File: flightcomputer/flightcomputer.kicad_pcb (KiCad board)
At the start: 2 copper layers, 100 x 100 mm, 48 parts, among them J1 Conn_Coaxial, J10 Conn_01x03, J11 Conn_01x03, J12 M20-6102045, J13 Conn_01x07, J2 Conn_Coaxial, J3 Conn_Coaxial, J4 Conn_Coaxial, U1 MAX-M10S, U2 LIS2MDLTR, U3 BMI088, U4 MS5607-02BA, U7 Teensy4.1, U8 LSM6DSO32TR, U9 RFM96W-433S2

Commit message: placement
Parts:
- removed D4, D5, D6: LED, LED_SMD:LED_0603_1608Metric_Pad1.05x0.95mm_HandSolder
- removed J13: Conn_01x07, Connector_Molex:Molex_SL_171971-0007_1x07_P2.54mm_Vertical
- removed R12, R13, R8: 500, Resistor_SMD:R_0603_1608Metric_Pad0.98x0.95mm_HandSolder
- removed R3, R4, R5, R6: 0, Resistor_SMD:R_0603_1608Metric_Pad0.98x0.95mm_HandSolder
- added BT1: 2998TR, HPRlibrary:BAT_2998TR, B.Cu at (69.7, 136.0)
- added C9: 1uF, Capacitor_SMD:C_0603_1608Metric_Pad1.08x0.95mm_HandSolder, F.Cu at (69.0, 111.0)
- added D10: ESD9B5.0ST5G, Diode_SMD:D_SOD-923, F.Cu at (262.4, 20.9)
- added D7: ESD9B5.0ST5G, Diode_SMD:D_SOD-923, F.Cu at (262.4, 15.0)
- added D8: ESD9B5.0ST5G, Diode_SMD:D_SOD-923, F.Cu at (262.4, 16.9)
- added D9: ESD9B5.0ST5G, Diode_SMD:D_SOD-923, F.Cu at (262.4, 18.9)
- added J5: S3B-PH-K-S-GW, HPRlibrary:S3BPHKSGW, F.Cu at (63.5, 87.0)
- added J6: S3B-PH-K-S-GW, HPRlibrary:S3BPHKSGW, F.Cu at (105.0, 132.6)
- added J7: S4B-PH-K-S_LF__SN_, HPRlibrary:S4B-PH-K-S_LF__SN_, F.Cu at (62.5, 98.0)
- added J8: S3B-PH-K-S-GW, HPRlibrary:S3BPHKSGW, F.Cu at (109.0, 79.5)
- added J9: Conn_01x06, Connector_PinHeader_2.54mm:PinHeader_1x06_P2.54mm_Vertical, F.Cu at (117.7, 122.0)
- added R14: 0, Resistor_SMD:R_0603_1608Metric_Pad0.98x0.95mm_HandSolder, F.Cu at (65.0, 127.2)
- added R15: 0, Resistor_SMD:R_0603_1608Metric_Pad0.98x0.95mm_HandSolder, F.Cu at (128.0, 83.9)
- added R16: 0, Resistor_SMD:R_0603_1608Metric_Pad0.98x0.95mm_HandSolder, F.Cu at (131.0, 83.9)
- added R17: 0, Resistor_SMD:R_0603_1608Metric_Pad0.98x0.95mm_HandSolder, F.Cu at (59.1, 110.0)
- added R7: 0, Resistor_SMD:R_0603_1608Metric_Pad0.98x0.95mm_HandSolder, F.Cu at (68.0, 127.2)
- added S1: EG1218, HPRlibrary:SW_EG1218, F.Cu at (60.0, 118.0)
- added TP10: TestPoint, Connector_PinHeader_2.54mm:PinHeader_1x01_P2.54mm_Vertical, F.Cu at (192.0, 43.2)
- added TP11: TestPoint, Connector_PinHeader_2.54mm:PinHeader_1x01_P2.54mm_Vertical, F.Cu at (192.0, 47.8)
- added TP12: TestPoint, Connector_PinHeader_2.54mm:PinHeader_1x01_P2.54mm_Vertical, F.Cu at (192.0, 52.4)
- added TP13: TestPoint, Connector_PinHeader_2.54mm:PinHeader_1x01_P2.54mm_Vertical, F.Cu at (192.0, 57.0)
- added TP14: TestPoint, Connector_PinHeader_2.54mm:PinHeader_1x01_P2.54mm_Vertical, F.Cu at (192.0, 34.0)
- added TP15: TestPoint, Connector_PinHeader_2.54mm:PinHeader_1x01_P2.54mm_Vertical, F.Cu at (115.0, 80.0)
- added TP16: TestPoint, Connector_PinHeader_2.54mm:PinHeader_1x01_P2.54mm_Vertical, F.Cu at (115.0, 75.4)
- added TP17: TestPoint, Connector_PinHeader_2.54mm:PinHeader_1x01_P2.54mm_Vertical, F.Cu at (99.0, 132.4)
- added TP18: TestPoint, Connector_PinHeader_2.54mm:PinHeader_1x01_P2.54mm_Vertical, F.Cu at (99.0, 137.0)
- added TP19: TestPoint, Connector_PinHeader_2.54mm:PinHeader_1x01_P2.54mm_Vertical, F.Cu at (70.0, 86.0)
- added TP2: TestPoint, Connector_PinSocket_2.54mm:PinSocket_1x01_P2.54mm_Vertical, F.Cu at (68.0, 108.0)
- added TP20: TestPoint, Connector_PinHeader_2.54mm:PinHeader_1x01_P2.54mm_Vertical, F.Cu at (70.0, 90.6)
- added TP21: TestPoint, Connector_PinHeader_2.54mm:PinHeader_1x01_P2.54mm_Vertical, F.Cu at (70.0, 102.6)
- added TP22: TestPoint, Connector_PinHeader_2.54mm:PinHeader_1x01_P2.54mm_Vertical, F.Cu at (70.0, 98.0)
- added TP3: TestPoint, Connector_PinHeader_2.54mm:PinHeader_1x01_P2.54mm_Vertical, F.Cu at (72.5, 108.0)
- added TP4: TestPoint, Connector_PinHeader_2.54mm:PinHeader_1x01_P2.54mm_Vertical, F.Cu at (110.0, 101.4)
- added TP5: TestPoint, Connector_PinHeader_2.54mm:PinHeader_1x01_P2.54mm_Vertical, F.Cu at (110.0, 92.4)
- added TP6: TestPoint, Connector_PinHeader_2.54mm:PinHeader_1x01_P2.54mm_Vertical, F.Cu at (110.0, 97.0)
- added TP7: TestPoint, Connector_PinHeader_2.54mm:PinHeader_1x01_P2.54mm_Vertical, F.Cu at (99.0, 80.0)
- added TP8: TestPoint, Connector_PinHeader_2.54mm:PinHeader_1x01_P2.54mm_Vertical, F.Cu at (99.0, 75.4)
- added TP9: TestPoint, Connector_PinHeader_2.54mm:PinHeader_1x01_P2.54mm_Vertical, F.Cu at (192.0, 38.6)
- C1, C2, C3, C4, C5, C6, C7, C8: footprint Capacitor_SMD:C_0402_1005Metric_Pad0.74x0.62mm_HandSolder -> Capacitor_SMD:C_0603_1608Metric_Pad1.08x0.95mm_HandSolder
- J12: footprint HPRfootprints:RHDR40W66P254_2X20_5146X500X1105P -> HPRlibrary:RHDR40W66P254_2X20_5146X500X1105P
- TP1: footprint Connector_Pin:Pin_D0.7mm_L6.5mm_W1.8mm_FlatFork -> Connector_PinSocket_2.54mm:PinSocket_1x01_P2.54mm_Vertical
- U2: footprint HPRfootprints:PQFN50P200X200X70-12N -> HPRlibrary:PQFN50P200X200X70-12N
- U3: footprint HPRfootprints:PQFN50P450X300X100-16N -> HPRlibrary:PQFN50P450X300X100-16N
- U7: footprint HPRfootprints:Teensy41 -> HPRlibrary:Teensy41
- U8: footprint HPRfootprints:XDCR_LSM6DSO32TR -> HPRlibrary:XDCR_LSM6DSO32TR
- U9: footprint HPRfootprints:MODULE_RFM96W-433S2 -> HPRlibrary:MODULE_RFM96W-433S2
- moved H4 128.6 mm to (61.0, 137.0)
- moved BZ1 123.5 mm to (72.0, 78.0), turned to 180 degrees
- moved J2 118.0 mm to (70.0, 135.0)
- moved R2 110.7 mm to (71.0, 127.2)
- moved R1 110.3 mm to (74.0, 127.2), turned to 90 degrees
- moved U8 88.2 mm to (103.0, 105.0), turned to 0 degrees
- moved U3 87.6 mm to (103.0, 98.0), turned to 0 degrees
- moved U1 87.2 mm to (69.0, 118.2), turned to -90 degrees
- moved U2 87.0 mm to (103.2, 91.2), turned to 0 degrees
- moved R11 84.7 mm to (100.1, 125.0), turned to 0 degrees
- moved C7 82.4 mm to (101.9, 108.0), turned to 180 degrees
- moved C8 79.6 mm to (105.9, 108.0)
- moved R9 77.1 mm to (100.0, 119.0), turned to 0 degrees
- moved H1 75.6 mm to (61.0, 75.0), turned to 0 degrees
- moved J1 73.6 mm to (59.0, 129.0), turned to 180 degrees
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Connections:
- C7 pad 1: Net-(U8-VDDIO) -> /teensy_3.3v
- C8 pad 1: Net-(U8-VDD) -> /teensy_3.3v
- J1 pad 1: Net-(J1-In) -> Net-(D7-A2)
- J10 pad 1: /ldo_5v -> /5V
- J10 pad 2: /ldo_5v -> /5V
- J10 pad 3: /ldo_5v -> /5V
- J2 pad 1: Net-(J1-In) -> Net-(D8-A2)
- J3 pad 1: Net-(J3-In) -> Net-(D9-A2)
- J4 pad 1: Net-(J3-In) -> Net-(D10-A2)
- R1 pad 1: /teensy_3.3v -> /gps_3.3v
- R2 pad 1: /teensy_3.3v -> /gps_3.3v
- TP1 pad 1: Net-(U7-VUSB) -> /radio_reset
- U1 pad 11: Net-(J1-In) -> Net-(U1-RF_IN)
- U1 pad 14: /teensy_3.3v -> unconnected-(U1-VCC_RF-Pad14)
- U1 pad 2: unconnected-(U1-TXD-Pad2) -> Net-(U1-TXD)
- U1 pad 3: unconnected-(U1-RXD-Pad3) -> Net-(U1-RXD)
- U1 pad 6: /teensy_3.3v -> /gps_vbckp
- U1 pad 7: /teensy_3.3v -> /gps_3.3v
- U1 pad 8: /teensy_3.3v -> /gps_3.3v
- U7 pad 10: /FREE1 -> /aux2_tx
- U7 pad 11: /FREE2 -> unconnected-(U7-9_OUT1C-Pad11)
- U7 pad 18: unconnected-(U7-26_A12_MOSI1-Pad18) -> /radio_mosi
- U7 pad 19: unconnected-(U7-27_A13_SCK1-Pad19) -> /radio_sck
- U7 pad 2: unconnected-(U7-0_RX1_CRX2_CS1-Pad2) -> /radio_cs
- U7 pad 20: unconnected-(U7-28_RX7-Pad20) -> /aux7_rx
- U7 pad 21: unconnected-(U7-29_TX7-Pad21) -> /aux7_tx
- U7 pad 22: unconnected-(U7-30_CRX3-Pad22) -> /can_rx
- U7 pad 23: unconnected-(U7-31_CTX3-Pad23) -> /can_tx
- U7 pad 24: unconnected-(U7-32_OUT1B-Pad24) -> /radio_reset
- U7 pad 25: unconnected-(U7-33_MCLK2-Pad25) -> /buzz_pwm
- U7 pad 26: /radio_dio3 -> /aux8_rx
- U7 pad 27: /radio_dio4 -> /aux8_tx
- U7 pad 3: unconnected-(U7-1_TX1_CTX2_MISO1-Pad3) -> /radio_miso
- U7 pad 31: /FREE6 -> unconnected-(U7-39_MISO1_OUT1A-Pad31)
- U7 pad 38: /FREE10 -> /aux1_scl
- U7 pad 39: /FREE9 -> /aux1_sda
- U7 pad 40: unconnected-(U7-18_A4_SDA-Pad40) -> /GPS_sda
- U7 pad 41: unconnected-(U7-19_A5_SCL-Pad41) -> /GPS_scl
- U7 pad 42: unconnected-(U7-20_A6_TX5_LRCLK1-Pad42) -> /GPS_reset
- U7 pad 43: unconnected-(U7-21_A7_RX5_BCLK1-Pad43) -> /GPS_int
- U7 pad 44: /FREE8 -> /lsmimu_cs
- U7 pad 45: /FREE7 -> /lsmimu_int
- U7 pad 49: Net-(U7-VUSB) -> unconnected-(U7-VUSB-Pad49)
- U7 pad 54: /teensy_onoff -> unconnected-(U7-ON_OFF-Pad54)
- U7 pad 7: /FREE11 -> unconnected-(U7-5_IN2-Pad7)
- U7 pad 8: /FREE12 -> unconnected-(U7-6_OUT1D-Pad8)
- U7 pad 9: /FREE5 -> /aux2_rx
- U8 pad 5: Net-(U8-VDDIO) -> /teensy_3.3v
- U8 pad 8: Net-(U8-VDD) -> /teensy_3.3v
- U9 pad 9: Net-(J3-In) -> Net-(U9-ANT)
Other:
- board size 100 x 100 mm -> 299 x 188 mm
- copper layers 2 -> 4

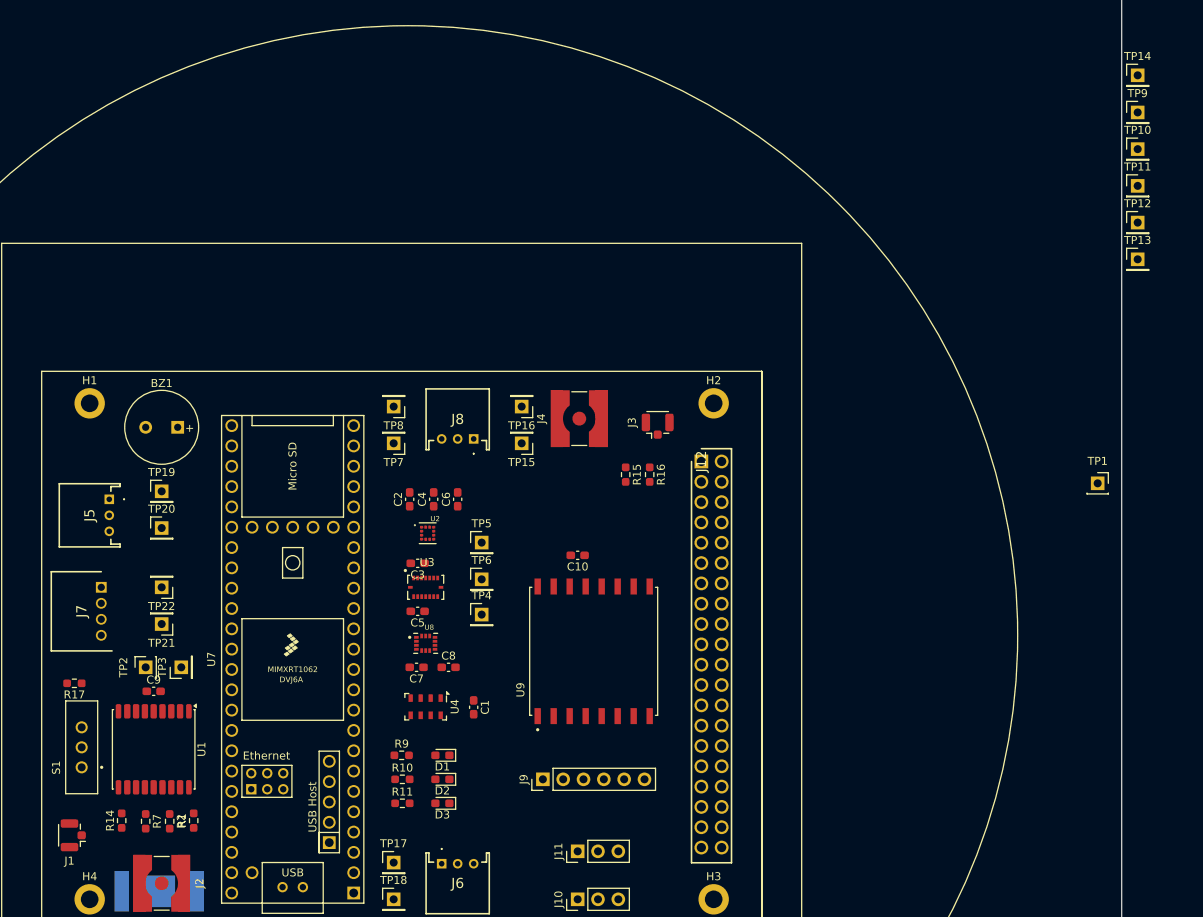
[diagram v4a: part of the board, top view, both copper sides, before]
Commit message: Y 0ohm for antenna selection
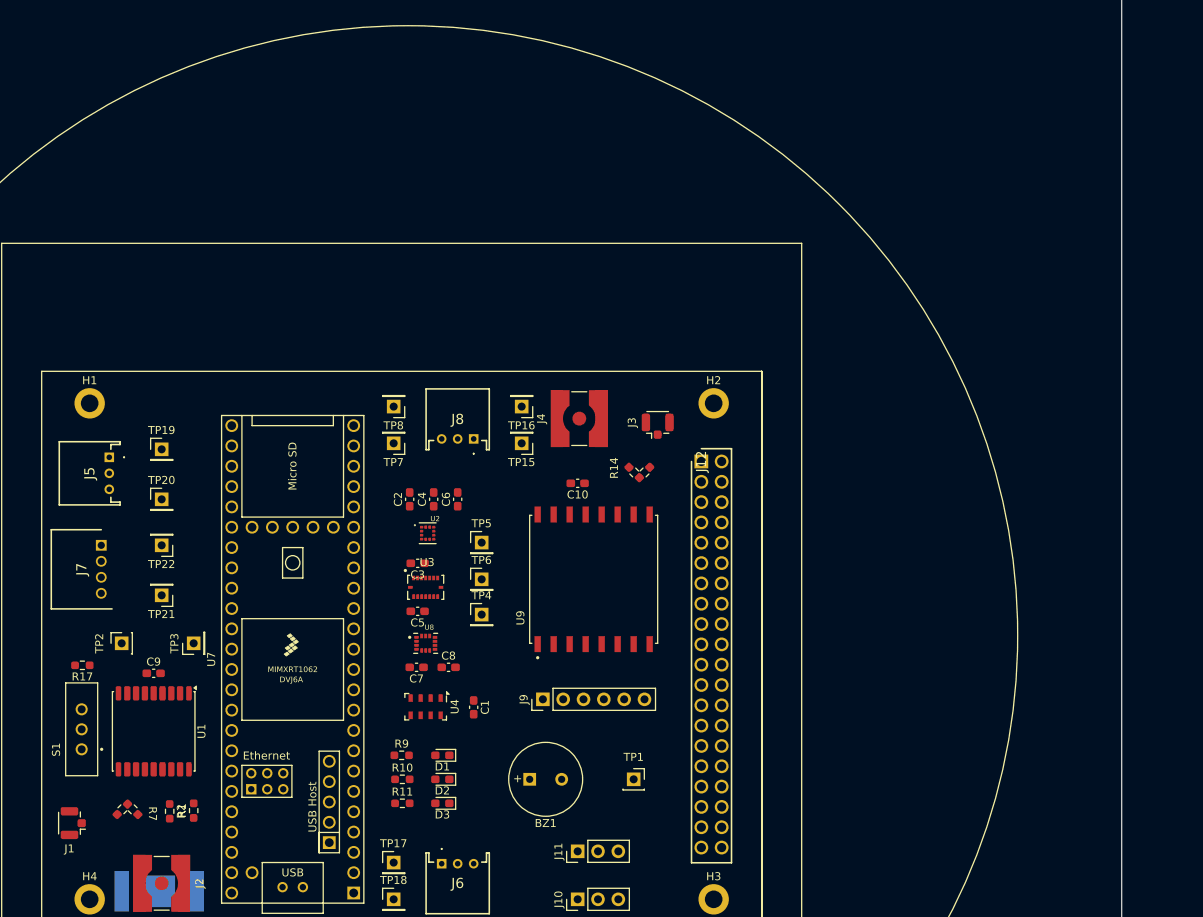
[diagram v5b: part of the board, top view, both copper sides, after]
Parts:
- removed R15, R16: 0, Resistor_SMD:R_0603_1608Metric_Pad0.98x0.95mm_HandSolder
- removed TP10, TP11, TP12, TP13, TP14, TP9: TestPoint, Connector_PinHeader_2.54mm:PinHeader_1x01_P2.54mm_Vertical
- R14, R7: footprint Resistor_SMD:R_0603_1608Metric_Pad0.98x0.95mm_HandSolder -> HPRlibrary:RES_0OHM_Y
- moved R14 76.1 mm to (127.1, 83.1)
- moved TP1 68.8 mm to (129.0, 122.0)
- moved BZ1 62.2 mm to (116.0, 122.0), turned to 0 degrees
- moved J9 10.0 mm to (117.7, 112.0)
- moved C10 9.00 mm to (122.0, 85.0)
- moved U9 9.00 mm to (124.0, 97.0)
- moved J5 5.25 mm to (63.5, 81.8)
- moved J7 5.25 mm to (62.5, 92.8)
- moved TP19 5.25 mm to (70.0, 80.8)
- moved TP22 5.25 mm to (70.0, 92.8)
- moved TP2 4.24 mm to (65.0, 105.0)
- moved TP20 3.59 mm to (70.0, 87.0)
- moved TP21 3.59 mm to (70.0, 99.0)
- moved TP3 3.38 mm to (74.0, 105.0)
- moved R17 2.46 mm to (60.1, 107.8)
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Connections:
- R14 pad 1: Net-(D7-A2) -> Net-(U9-ANT)
- R14 pad 2: Net-(U1-RF_IN) -> Net-(D10-A2)
- U7 pad 11: unconnected-(U7-9_OUT1C-Pad11) -> /buzz_pwm
- U7 pad 25: /buzz_pwm -> unconnected-(U7-33_MCLK2-Pad25)
